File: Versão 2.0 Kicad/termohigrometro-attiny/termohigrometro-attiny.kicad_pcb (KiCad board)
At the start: 2 copper layers, 100 x 85 mm, 19 parts, among them J1 Conn_02x03_Odd_Even, J3 Chave, J4 Screw_Terminal_01x04, J5 Screw_Terminal_01x04, J6 Carregador, U1 ATtiny85-20P, U2 AMS1117-3.3

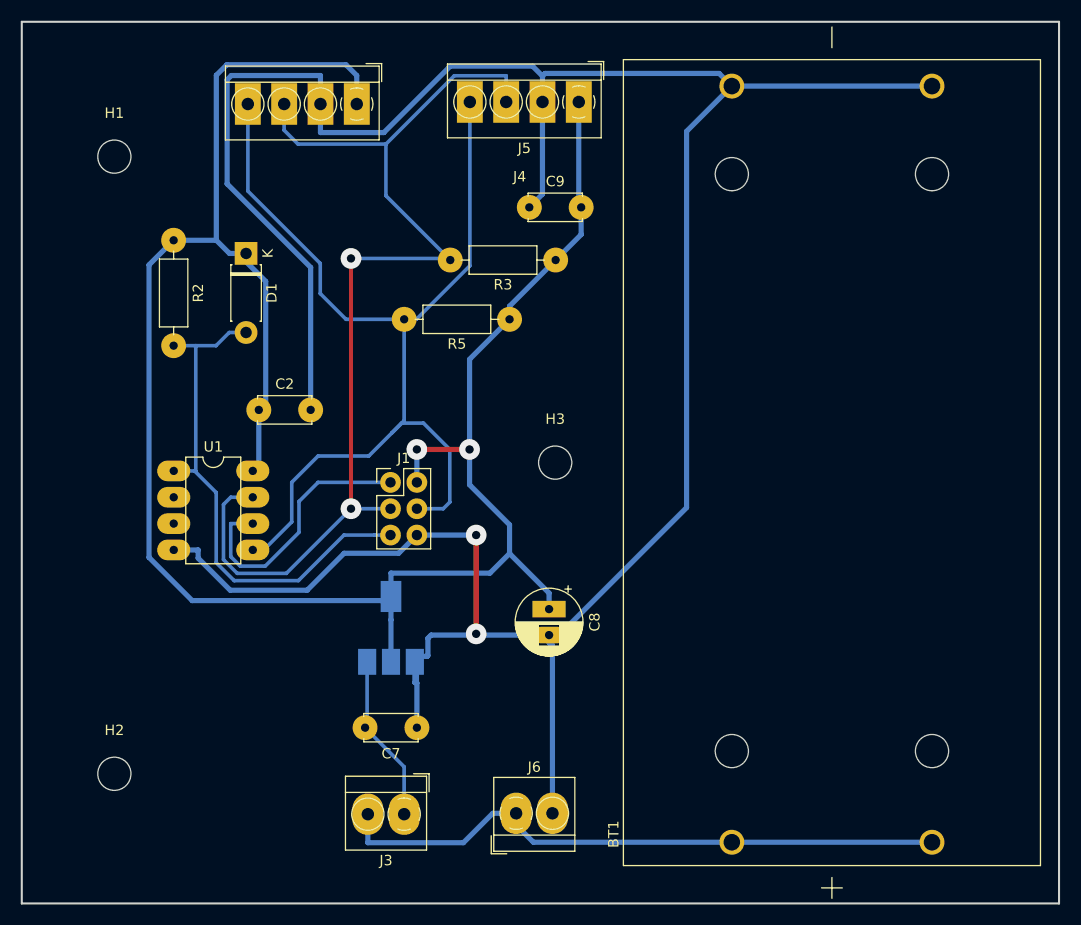
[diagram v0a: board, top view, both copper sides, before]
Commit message: placa com attiny
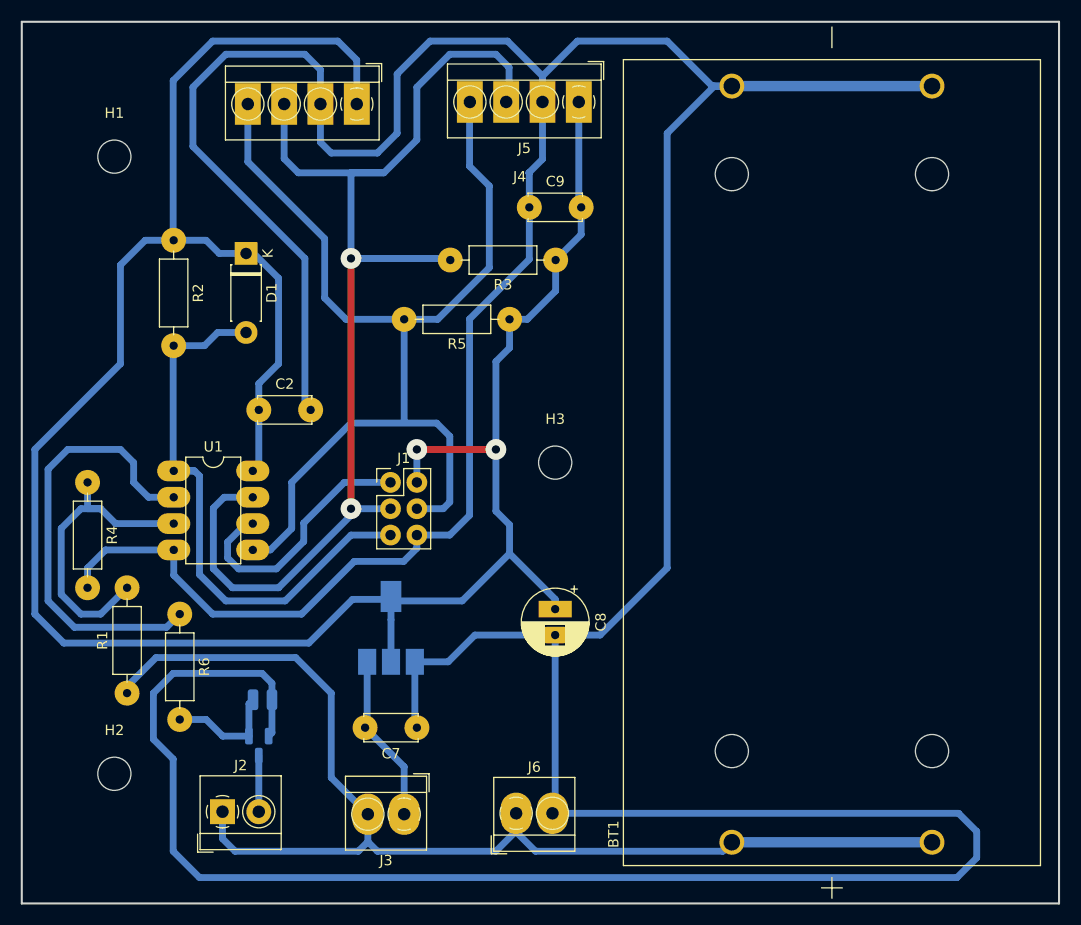
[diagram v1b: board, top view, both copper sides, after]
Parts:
- added J2: Fan, TerminalBlock_4Ucon:TerminalBlock_4Ucon_1x02_P3.50mm_Horizontal, F.Cu at (115.2, 124.5)
- added Q1: 2N7002K, Package_TO_SOT_SMD:SOT-23, B.Cu at (118.7, 118.1)
- added R1: 1M, Resistor_THT:R_Axial_DIN0207_L6.3mm_D2.5mm_P10.16mm_Horizontal, F.Cu at (106.0, 113.0)
- added R4: 1M, Resistor_THT:R_Axial_DIN0207_L6.3mm_D2.5mm_P10.16mm_Horizontal, F.Cu at (102.2, 92.7)
- added R6: 100, Resistor_THT:R_Axial_DIN0207_L6.3mm_D2.5mm_P10.16mm_Horizontal, F.Cu at (111.1, 105.4)
- added R7: 10k, Resistor_SMD:R_0805_2012Metric, B.Cu at (119.1, 113.7)
- moved C8 0.59 mm to (147.3, 104.9)
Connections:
- U1 pad 2: unconnected-(U1-Pad2) -> FAN
- U1 pad 3: unconnected-(U1-Pad3) -> VBS
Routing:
- net GND: track 270.4 -> 481.4 mm, vias 2 -> 0
- net +BATT: track 60.6 -> 116.4 mm
- net FAN: track 0.00 -> 42.9 mm
- net +3V3: track 205.5 -> 238.5 mm
- net VBS: track 0.00 -> 30.6 mm
- net SCK: track 104.6 -> 126.0 mm
- net Net-(Q1-Pad1): track 0.00 -> 11.0 mm
- net Net-(J2-Pad2): track 0.00 -> 5.41 mm
- net RST: track 50.8 -> 55.9 mm
- net MOSI: track 101.8 -> 104.3 mm
- net MISO: track 26.2 -> 25.3 mm

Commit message: adicionado capacitor na leitura de tensão. Alterado ligação da bateria
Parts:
- added C1: 220n, Capacitor_THT:C_Disc_D5.0mm_W2.5mm_P5.00mm, F.Cu at (106.4, 97.7)
- added D2: D, Diode_THT:D_DO-41_SOD81_P7.62mm_Horizontal, F.Cu at (138.1, 116.9)
- R1: value 1M -> 2M
- moved U1 2.10 mm to (112.6, 91.7)
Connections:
- BT1 pad 1-: GND -> Net-(BT1-Pad1-)
- BT1 pad 2+: +BATT -> Net-(BT1-Pad1-)
- J3 pad 1: Net-(C7-Pad2) -> Net-(J3-Pad1)
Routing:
- net Net-(BT1-Pad1-): track 0.00 -> 86.1 mm
- net GND: track 481.4 -> 450.9 mm
- net +BATT: track 116.4 -> 97.8 mm
- net Net-(J3-Pad1): track 0.00 -> 5.44 mm
- net Net-(C7-Pad2): track 16.3 -> 21.3 mm
- net VBS: track 30.6 -> 33.8 mm
- net FAN: track 42.9 -> 45.8 mm
- net RST: track 55.9 -> 54.0 mm
- net MISO: track 25.3 -> 26.7 mm
- net +3V3: track 238.5 -> 239.4 mm
- net MOSI: track 104.3 -> 103.5 mm
